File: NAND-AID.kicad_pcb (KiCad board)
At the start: 2 copper layers, 33.7 x 21.4 mm, 21 parts

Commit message: Fix library
Signed-off-by: Thomas Rohloff <v10lator@myway.de>
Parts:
- ? (x7): footprint V10lator's footprints:Small Half Hole -> NAND-AID:Small Half Hole
- ? (x4): footprint V10lator's footprints:Dump Pad with VIA -> NAND-AID:Dump Pad with VIA
- ?: value Voultar's Micro SD -> Micro SD slot; footprint V10lator's footprints:Voultar's Micro SD -> NAND-AID:Micro SD slot
- ? (x3): footprint V10lator's footprints:Dump Pad no VIA -> NAND-AID:Dump Pad no VIA
- ?: footprint V10lator's footprints:GND hole -> NAND-AID:GND hole
- ?: footprint V10lator's footprints:3V3 Pad -> NAND-AID:3V3 Pad
- ?: footprint V10lator's footprints:GND Half Hole -> NAND-AID:GND Half Hole
- C1: footprint V10lator's footprints:C_0805_2012Metric NO SILKSCREEN -> NAND-AID:C_0805_2012Metric NO SILKSCREEN
- DSB: footprint V10lator's footprints:SolderJumper-2_P1.3mm_Open_TrianglePad1.0x1.5mm EDITED SILKSCREEN -> NAND-AID:SolderJumper-2_P1.3mm_Open_TrianglePad1.0x1.5mm EDITED SILKSCREEN
- G***: footprint V10lator's footprints:LOGO Toad -> NAND-AID:LOGO Toad
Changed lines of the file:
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@@
   (net 8 "CLK")
   (net 9 "DUMMY")
-  (footprint "V10lator's footprints:Small Half Hole" (layer "F.Cu")
+  (footprint "NAND-AID:Small Half Hole" (layer "F.Cu")
     (at 136.19 109.198)
     (fp_text reference "" (at 0 0) (layer "F.SilkS")
@@
       (net 7 "CMD"))
   )
-  (footprint "V10lator's footprints:Dump Pad with VIA" (layer "F.Cu")
+  (footprint "NAND-AID:Dump Pad with VIA" (layer "F.Cu")
     (at 144.032 109.705)
     (fp_text reference "" (at 0 0) (layer "F.SilkS")
@@
       (net 6 "D3"))
   )
-  (footprint "V10lator's footprints:Dump Pad no VIA" (layer "F.Cu")
+  (footprint "NAND-AID:Dump Pad no VIA" (layer "F.Cu")
     (at 149.112 109.705)
     (attr smd board_only)
@@
       (net 9 "DUMMY"))
   )
-  (footprint "V10lator's footprints:Dump Pad no VIA" (layer "F.Cu")
+  (footprint "NAND-AID:Dump Pad no VIA" (layer "F.Cu")
     (at 146.572 109.705)
     (attr smd board_only)
@@
       (net 7 "CMD"))
   )
-  (footprint "V10lator's footprints:3V3 Pad" (layer "F.Cu")
+  (footprint "NAND-AID:3V3 Pad" (layer "F.Cu")
     (at 132.588 110.12)
     (fp_text reference "" (at 0 0) (layer "F.SilkS")
@@
       (net 1 "3V3"))
   )
-  (footprint "V10lator's footprints:Small Half Hole" (layer "F.Cu")
+  (footprint "NAND-AID:Small Half Hole" (layer "F.Cu")
     (at 137.592 109.198)
     (fp_text reference "" (at 0 0) (layer "F.SilkS")
@@
       (net 8 "CLK"))
   )
-  (footprint "V10lator's footprints:Small Half Hole" (layer "F.Cu")
+  (footprint "NAND-AID:Small Half Hole" (layer "F.Cu")
     (at 131.99 109.198)
     (fp_text reference "" (at 0 0) (layer "F.SilkS")
@@
       (net 4 "D1"))
   )
-  (footprint "V10lator's footprints:SolderJumper-2_P1.3mm_Open_TrianglePad1.0x1.5mm EDITED SILKSCREEN" (layer "F.Cu")
+  (footprint "NAND-AID:SolderJumper-2_P1.3mm_Open_TrianglePad1.0x1.5mm EDITED SILKSCREEN" (layer "F.Cu")
     (at 140.724 105.625)
     (descr "SMD Solder Jumper, 1x1.5mm Triangular Pads, 0.3mm gap, open")
@@
       ))
   )
-  (footprint "V10lator's footprints:LOGO Toad" (layer "F.Cu")
+  (footprint "NAND-AID:LOGO Toad" (layer "F.Cu")
     (at 146.2 99.1854)
     (attr board_only exclude_from_pos_files exclude_from_bom)
@@
       ))
   )
-  (footprint "V10lator's footprints:C_0805_2012Metric NO SILKSCREEN" (layer "F.Cu")
+  (footprint "NAND-AID:C_0805_2012Metric NO SILKSCREEN" (layer "F.Cu")
     (at 151.767 106.778)
     (descr "Capacitor SMD 0805 (2012 Metric), square (rectangular) end terminal, IPC_7351 nominal, (Body size source: IPC-SM-782 page 76, https://www.pcb-3d.com/wordpress/wp-content/uploads/ipc-sm-782a_amendment_1_and_2.pdf, https://docs.google.com/spreadsheets/d/1BsfQQcO9C6DZCsRaXUlFlo91Tg2WpOkGARC1WS5S8t0/edit?usp=sharing), generated with kicad-footprint-generator")
@@
     )
   )
-  (footprint "V10lator's footprints:GND Half Hole" (layer "F.Cu")
+  (footprint "NAND-AID:GND Half Hole" (layer "F.Cu")
     (at 163.21 96.403)
     (fp_text reference "" (at 0 0) (layer "F.SilkS")
@@
       (net 2 "GND") (zone_connect 2))
   )
-  (footprint "V10lator's footprints:Dump Pad with VIA" (layer "F.Cu")
+  (footprint "NAND-AID:Dump Pad with VIA" (layer "F.Cu")
     (at 136.412 109.705)
     (fp_text reference "" (at 0 0) (layer "F.SilkS")
@@
       (net 5 "D2"))
   )
-  (footprint "V10lator's footprints:Small Half Hole" (layer "F.Cu")
+  (footprint "NAND-AID:Small Half Hole" (layer "F.Cu")
     (at 137.592 107.905)
     (fp_text reference "" (at 0 0) (layer "F.SilkS")
@@
       (net 9 "DUMMY"))
   )
-  (footprint "V10lator's footprints:Dump Pad with VIA" (layer "F.Cu")
+  (footprint "NAND-AID:Dump Pad with VIA" (layer "F.Cu")
     (at 141.492 109.705)
     (fp_text reference "" (at 0 0) (layer "F.SilkS")
@@
       (net 3 "D0"))
   )
-  (footprint "V10lator's footprints:Dump Pad with VIA" (layer "F.Cu")
+  (footprint "NAND-AID:Dump Pad with VIA" (layer "F.Cu")
     (at 138.952 109.705)
     (fp_text reference "" (at 0 0) (layer "F.SilkS")
@@
       (net 4 "D1"))
   )
-  (footprint "V10lator's footprints:Voultar's Micro SD" (layer "F.Cu")
+  (footprint "NAND-AID:Micro SD slot" (layer "F.Cu")
     (at 149.837 99.059999)
+    (clearance -0.2)
     (fp_text reference "" (at 0 -0.5 unlocked) (layer "F.SilkS") hide
         (effects (font (size 1 1) (thickness 0.1)))
     )
-    (fp_text value "Voultar's Micro SD" (at 0 1 unlocked) (layer "F.Fab")
+    (fp_text value "Micro SD slot" (at 0 1 unlocked) (layer "F.Fab")
         (effects (font (size 1 1) (thickness 0.15)))
     )
@@
       (net 2 "GND") (zone_connect 2))
   )
-  (footprint "V10lator's footprints:Small Half Hole" (layer "F.Cu")
+  (footprint "NAND-AID:Small Half Hole" (layer "F.Cu")
     (at 133.392 109.198)
     (fp_text reference "" (at 0 0) (layer "F.SilkS")
@@
       (net 3 "D0"))
   )
-  (footprint "V10lator's footprints:Dump Pad no VIA" (layer "F.Cu")
+  (footprint "NAND-AID:Dump Pad no VIA" (layer "F.Cu")
     (at 152.322 109.705)
     (attr smd board_only)
@@
       (net 2 "GND") (zone_connect 2))
   )
-  (footprint "V10lator's footprints:Small Half Hole" (layer "F.Cu")
+  (footprint "NAND-AID:Small Half Hole" (layer "F.Cu")
     (at 134.791 109.198)
     (fp_text reference "" (at 0 0) (layer "F.SilkS")
@@
       (net 6 "D3"))
   )
-  (footprint "V10lator's footprints:Small Half Hole" (layer "F.Cu")
+  (footprint "NAND-AID:Small Half Hole" (layer "F.Cu")
     (at 130.591 109.198)
     (fp_text reference "" (at 0 0) (layer "F.SilkS")
@@
       (net 5 "D2"))
   )
-  (footprint "V10lator's footprints:GND hole" (layer "F.Cu")
+  (footprint "NAND-AID:GND hole" (layer "F.Cu")
     (at 154.487 96.6026)
     (attr allow_missing_courtyard)

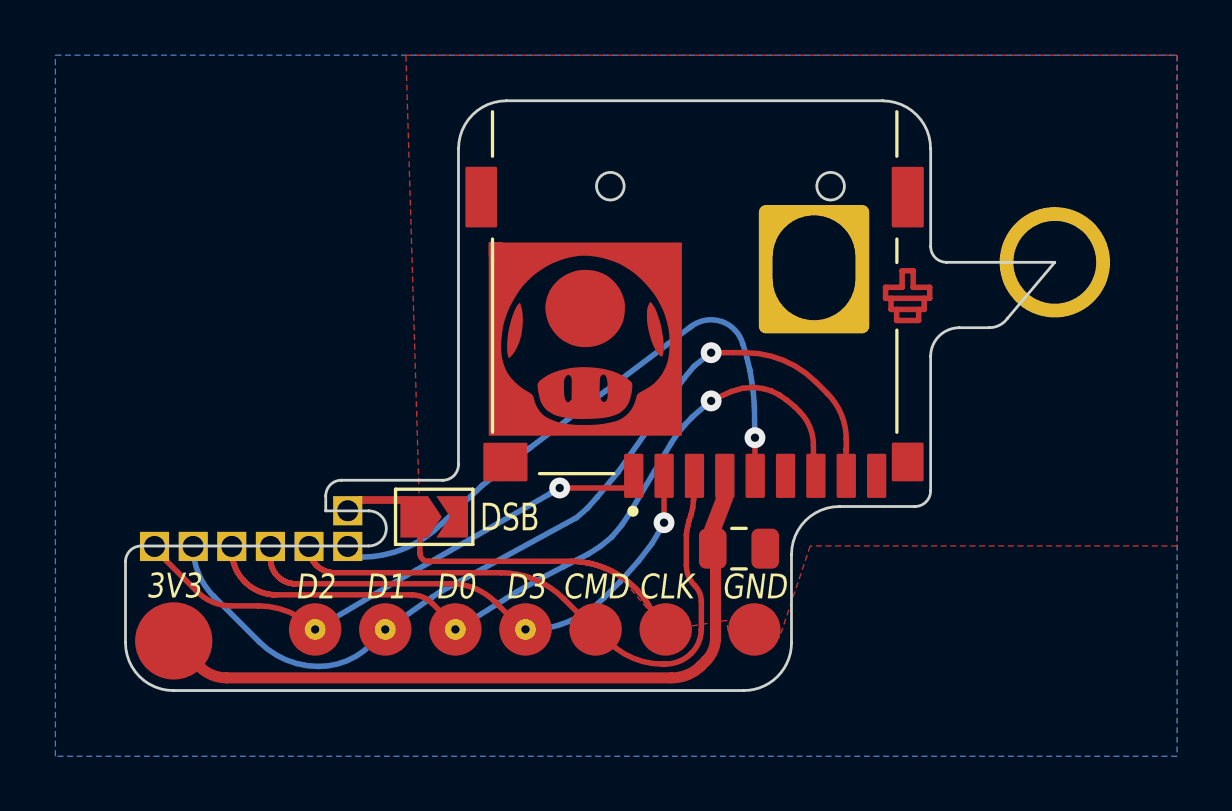
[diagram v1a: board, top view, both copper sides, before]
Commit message: Change keepout zones
This makes it more like the RE-ed GND fill and might also make it more simple to transform into manufacuting data from the gerber file. Also it reduces polygone and zone usage to a minimum.

Signed-off-by: Thomas Rohloff <v10lator@myway.de>
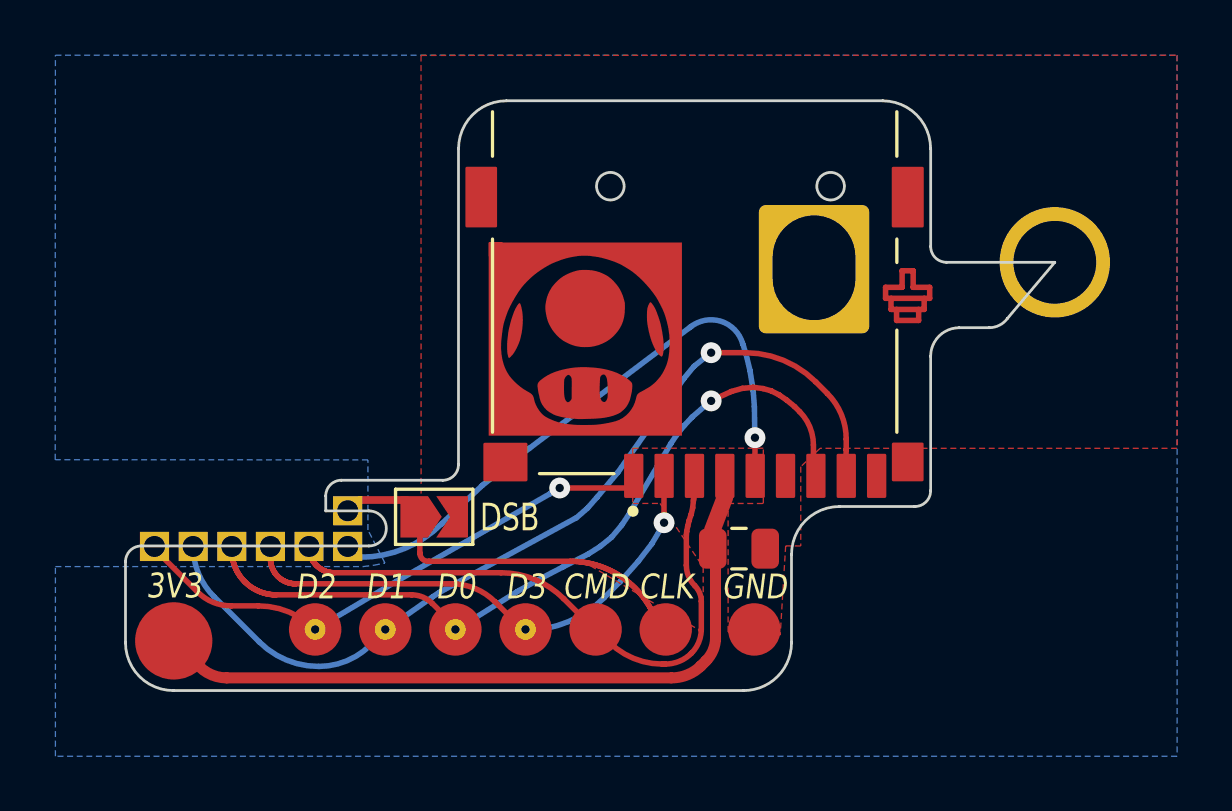
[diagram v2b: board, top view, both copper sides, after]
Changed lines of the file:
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@@
     (polygon
       (pts
-        (xy 139.7 88.9)
+        (xy 140.247821 88.907569)
         (xy 167.64 88.9)
-        (xy 167.64 106.68)
-        (xy 154.349416 106.68)
-        (xy 153.235405 109.995028)
-        (xy 151.37586 109.763154)
-        (xy 151.315915 109.375486)
-        (xy 149.112 109.735)
-        (xy 147.362636 107.677116)
-        (xy 145.963014 107.247166)
+        (xy 167.640989 103.143441)
+        (xy 154.704415 103.14269)
+        (xy 154.005249 103.808101)
+        (xy 154.005513 106.68)
+        (xy 153.457951 106.678736)
+        (xy 153.260843 109.909625)
+        (xy 151.372391 109.79964)
+        (xy 151.371671 105.140845)
+        (xy 152.648673 105.141236)
+        (xy 152.648673 103.138764)
+        (xy 147.919321 103.13924)
+        (xy 147.917242 105.139782)
+        (xy 148.907935 105.139782)
+        (xy 150.469659 107.442074)
+        (xy 150.470636 109.813674)
+        (xy 146.081765 107.217134)
         (xy 140.249495 107.214684)
       )
@@
     )
   )
-  (zone (net 0) (net_name "") (layer "F.Cu") (hatch edge 0.5)
-    (connect_pads (clearance 0))
-    (min_thickness 0.25) (filled_areas_thickness no)
-    (keepout (tracks allowed) (vias allowed) (pads allowed) (copperpour not_allowed) (footprints allowed))
-    (fill (thermal_gap 0.5) (thermal_bridge_width 0.5))
-    (polygon
-      (pts
-        (xy 149.230044 104.801453)
-        (xy 149.985991 104.801454)
-        (xy 149.985991 105.762137)
-        (xy 149.230044 105.762136)
-      )
-    )
-  )
-  (zone (net 0) (net_name "") (layer "B.Cu") (hatch edge 0.5)
-    (connect_pads (clearance 0))
-    (min_thickness 0.25) (filled_areas_thickness no)
-    (keepout (tracks allowed) (vias allowed) (pads allowed) (copperpour not_allowed) (footprints allowed))
-    (fill (thermal_gap 0.5) (thermal_bridge_width 0.5))
-    (polygon
-      (pts
-        (xy 135.784542 103.562296)
-        (xy 138.324542 103.562296)
-        (xy 138.324542 106.102296)
-        (xy 135.784542 106.102296)
-      )
-    )
-  )
   (zone (net 2) (net_name "GND") (layer "B.Cu") (hatch edge 0.5)
     (connect_pads (clearance 0))
@@
     (polygon
       (pts
+        (xy 127 107.4288)
+        (xy 138.151828 107.427386)
+        (xy 138.54153 107.378238)
+        (xy 138.939959 107.300656)
+        (xy 138.324542 106.102296)
+        (xy 138.324542 103.562296)
+        (xy 126.9935 103.5556)
         (xy 127 88.9)
         (xy 167.64 88.9)
@@
       )
     )
-  )
-  (zone (net 0) (net_name "") (layer "B.Cu") (hatch edge 0.5)
-    (connect_pads (clearance 0))
-    (min_thickness 0.25) (filled_areas_thickness no)
-    (keepout (tracks allowed) (vias allowed) (pads allowed) (copperpour not_allowed) (footprints allowed))
-    (fill (thermal_gap 0.5) (thermal_bridge_width 0.5))
-    (polygon
-      (pts
-        (xy 129.46516 107.427386)
-        (xy 138.151828 107.427386)
-        (xy 138.454357 107.386609)
-        (xy 138.758786 107.302821)
-        (xy 138.987464 107.184683)
-        (xy 139.7 106.68)
-        (xy 129.54 106.68)
-      )
-    )

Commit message: Move GND hole a tiny bit down
This brings it in line with the new spacing.

Signed-off-by: Thomas Rohloff <v10lator@myway.de>
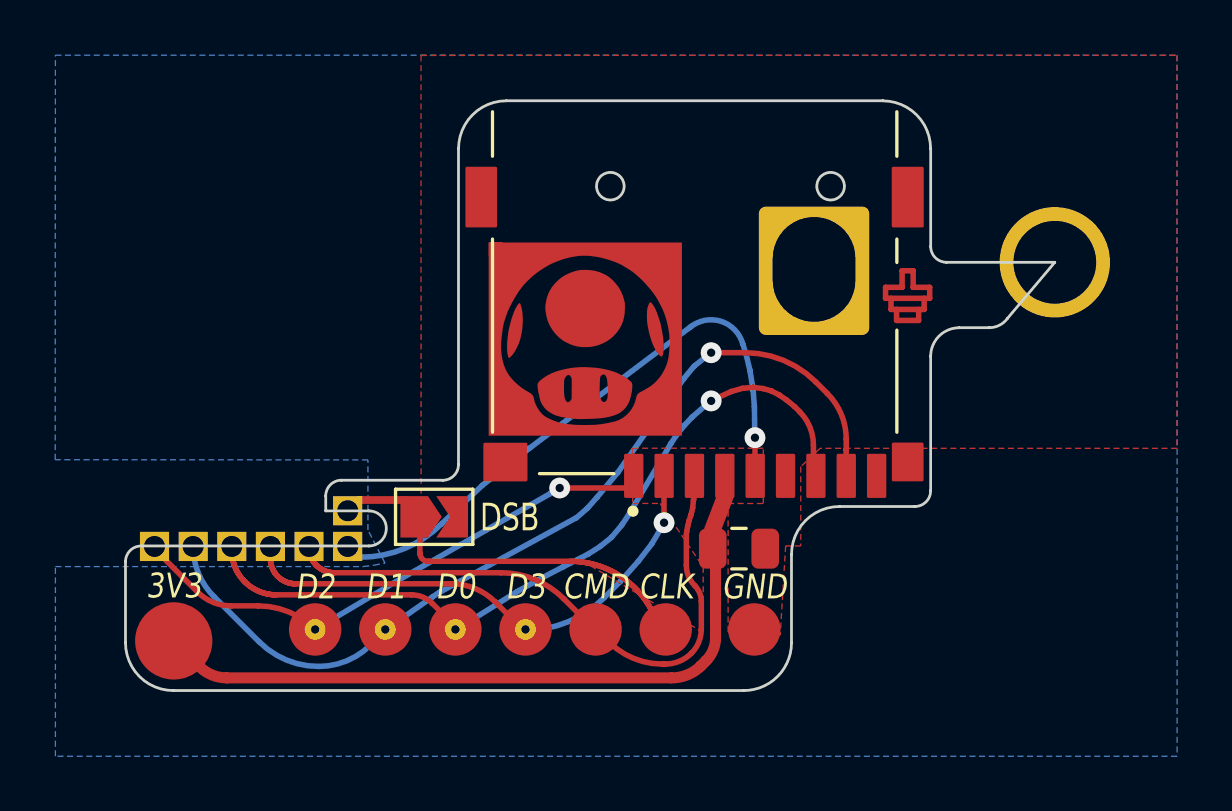
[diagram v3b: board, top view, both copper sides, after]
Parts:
- moved ? 0.06 mm to (154.5, 96.7)
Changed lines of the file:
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@@
   )
   (footprint "NAND-AID:GND hole" (layer "F.Cu")
-    (at 154.487 96.6026)
+    (at 154.487 96.66)
     (attr allow_missing_courtyard)
     (fp_text reference "" (at 0 0) (layer "F.SilkS")

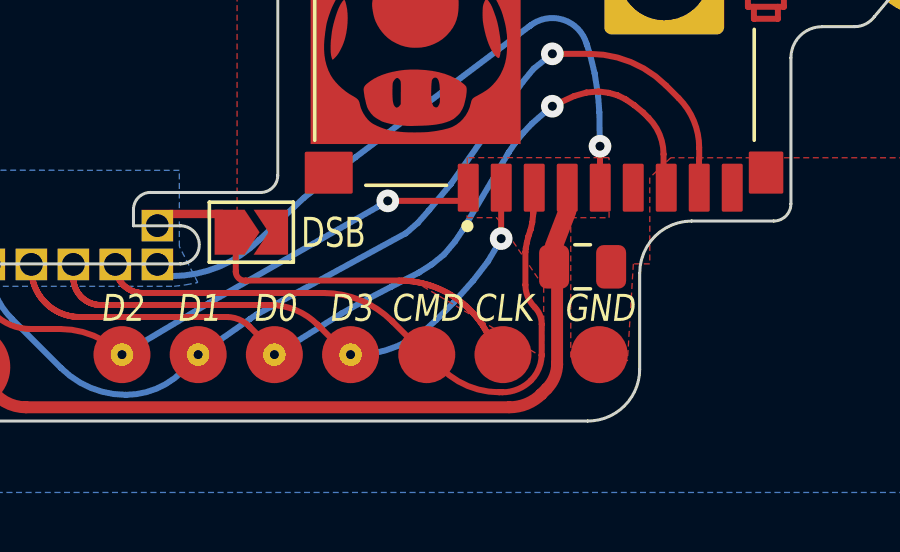
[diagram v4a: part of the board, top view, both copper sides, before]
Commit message: Enable a few more teardrops
Signed-off-by: Thomas Rohloff <v10lator@myway.de>
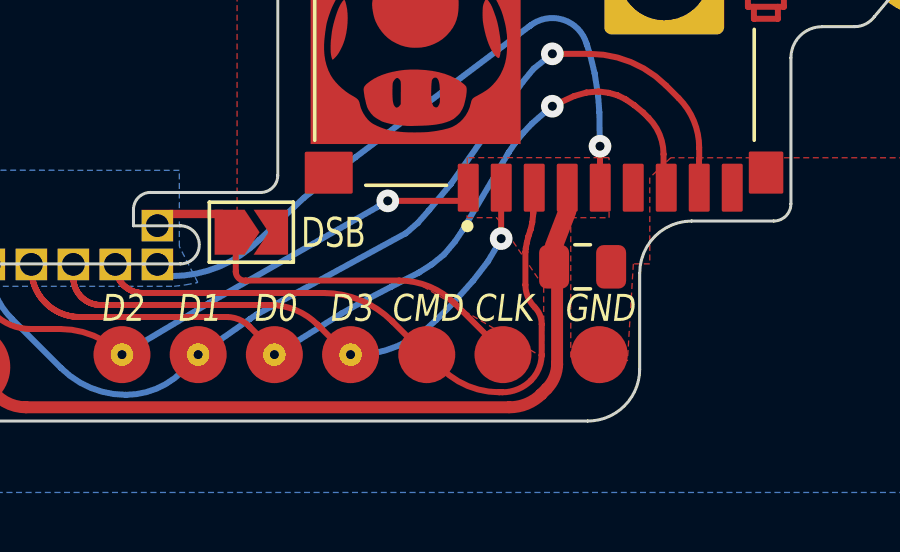
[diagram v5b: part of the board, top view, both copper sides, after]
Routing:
- net DUMMY: track 11.8 -> 12.3 mm

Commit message: Add some thermal reliefs
Signed-off-by: Thomas Rohloff <v10lator@myway.de>
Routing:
- net GND: track 8.80 -> 15.2 mm
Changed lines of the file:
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@@
       (stroke (width 0.1) (type default)) (fill none) (layer "Edge.Cuts"))
     (pad "" smd roundrect (at -7.655326 -4.269797) (size 1.149336 2.19831) (drill (offset 0.247744 -0.749823)) (layers "F.Cu" "F.Paste" "F.Mask") (roundrect_rratio 0.04171756209)
-      (net 2 "GND") (zone_connect 2))
+      (net 2 "GND") (zone_connect 1) (thermal_bridge_width 0.2) (thermal_gap 0.2))
     (pad "" smd roundrect (at -6.975213 4.914618) (size 1.600302 1.399965) (drill (offset 0.442643 -0.334279)) (layers "F.Cu" "F.Paste" "F.Mask") (roundrect_rratio 0.03571517859)
-      (net 2 "GND") (zone_connect 2))
+      (net 2 "GND") (zone_connect 1) (thermal_bridge_width 0.2) (thermal_gap 0.2))
     (pad "" smd roundrect (at -2.18009 5.82752) (size 0.7006 1.600516) (drill (offset 0.297355 -0.747276)) (layers "F.Cu" "F.Paste" "F.Mask") (roundrect_rratio 0.07136739937)
       (net 5 "D2"))
@@
     (pad "" smd roundrect (at 6.61974 5.82752) (size 0.7006 1.600516) (drill (offset 0.297355 -0.747276)) (layers "F.Cu" "F.Paste" "F.Mask") (roundrect_rratio 0.07136739937))
     (pad "" smd roundrect (at 7.5964 5.08) (size 1.15134 1.404587) (drill (offset 0.447873 -0.503524)) (layers "F.Cu" "F.Paste" "F.Mask") (roundrect_rratio 0.04171742286)
-      (net 2 "GND") (zone_connect 2))
+      (net 2 "GND") (zone_connect 1) (thermal_bridge_width 0.4) (thermal_gap 0.2))
     (pad "" smd roundrect (at 7.797343 -4.268633) (size 1.161236 2.19831) (drill (offset 0.247744 -0.749823)) (layers "F.Cu" "F.Paste" "F.Mask") (roundrect_rratio 0.04171756209)
-      (net 2 "GND") (zone_connect 2))
+      (net 2 "GND") (zone_connect 1) (thermal_bridge_width 0.2) (thermal_gap 0.2))
   )
   (footprint "NAND-AID:Small Half Hole" (layer "F.Cu")
@@
     )
     (pad "" thru_hole roundrect (at 0 0) (size 4 4.65) (drill oval 3 3.8 (offset 0 0.05)) (property pad_prop_castellated) (layers "*.Cu" "*.Mask") (roundrect_rratio 0.0625)
-      (net 2 "GND") (solder_mask_margin 0.0001) (zone_connect 2))
+      (net 2 "GND") (solder_mask_margin 0.0001) (zone_connect 1) (thermal_bridge_width 0.755) (thermal_gap 0.15))
   )
   (gr_poly
@@
   (segment (start 158.077221 97.309854) (end 158.077382 96.7101) (width 0.2) (layer "F.Cu") (net 2))
   (segment (start 157.077 97.7088) (end 158.676 97.708832) (width 0.2) (layer "F.Cu") (net 2))
+  (segment (start 154.487 96.66) (end 156.613639 99.240934) (width 0.755) (layer "F.Cu") (net 2))
   (segment (start 157.676958 97.309854) (end 157.677122 96.7101) (width 0.2) (layer "F.Cu") (net 2))
   (segment (start 158.676474 97.3099) (end 158.676474 97.7088) (width 0.2) (layer "F.Cu") (net 2))
+  (segment (start 154.487 96.66) (end 152.492049 99.017263) (width 0.755) (layer "F.Cu") (net 2))
   (segment (start 158.077221 97.309854) (end 158.676 97.3099) (width 0.2) (layer "F.Cu") (net 2))
   (segment (start 157.076854 97.3099) (end 157.076854 97.7088) (width 0.2) (layer "F.Cu") (net 2))
@@
     (polygon
       (pts
+        (xy 140.24824 93.484349)
+        (xy 142.87213 93.482247)
+        (xy 142.871515 92.739874)
+        (xy 140.247292 92.739874)
         (xy 140.247821 88.907569)
-        (xy 167.64 88.9)
+        (xy 160.791956 88.901892)
+        (xy 160.794624 92.740463)
+        (xy 157.526355 92.742056)
+        (xy 157.525703 93.596152)
+        (xy 167.64 93.591684)
         (xy 167.640989 103.143441)
         (xy 154.704415 103.14269)
@@
       )
     )
+  )
+  (zone (net 0) (net_name "") (layer "F.Cu") (hatch edge 0.5)
+    (connect_pads (clearance 0))
+    (min_thickness 0.25) (filled_areas_thickness no)
+    (keepout (tracks allowed) (vias allowed) (pads allowed) (copperpour not_allowed) (footprints allowed))
+    (fill (thermal_gap 0.5) (thermal_bridge_width 0.5))
+    (polygon
+      (pts
+        (xy 142.304748 103.332769)
+        (xy 143.644664 103.333905)
+        (xy 143.64539 104.540681)
+        (xy 142.629016 104.539974)
+        (xy 142.304759 104.207031)
+      )
+    )
